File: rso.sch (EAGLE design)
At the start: 24 parts, among them X10 1-227161-0, X6 1-227161-0, X7 1-227161-0, X8 1-227161-0, X9 1-227161-0

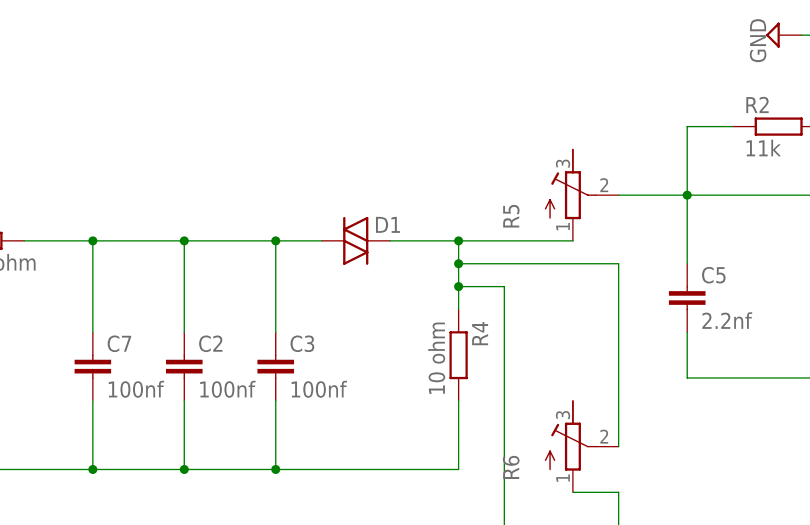
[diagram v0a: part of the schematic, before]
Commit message: CHanges to the thikness of the tracks
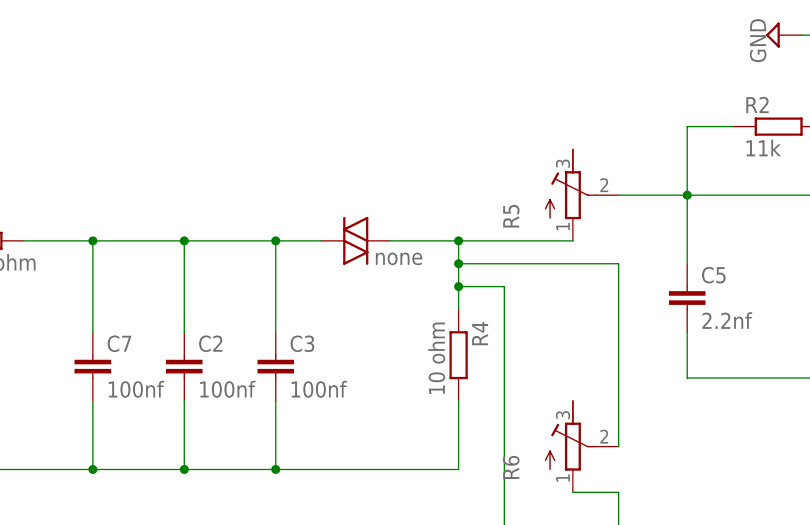
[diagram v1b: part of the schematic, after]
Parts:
- D1: value (none) -> none
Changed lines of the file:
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@@
 <classes>
 <class number="0" name="default" width="0" drill="0">
+<clearance class="0" value="0.205"/>
 </class>
 </classes>
@@
 <attribute name="RS_NUMBER" value="178-1862"/>
 </part>
-<part name="D1" library="diode" library_urn="urn:adsk.eagle:library:210" deviceset="DIAC-" device="DO35-10" package3d_urn="urn:adsk.eagle:package:43344/2">
+<part name="D1" library="diode" library_urn="urn:adsk.eagle:library:210" deviceset="DIAC-" device="DO35-10" package3d_urn="urn:adsk.eagle:package:43344/2" value="none">
 <attribute name="MF" value="NTE ELECTRONICS"/>
 <attribute name="MPN" value="NTE6408"/>
@@
 </instance>
 <instance part="D1" gate="-B1" x="-30.48" y="172.72" smashed="yes">
-<attribute name="NAME" x="-29.718" y="173.609" size="1.778" layer="95"/>
+<attribute name="NAME" x="-29.718" y="173.609" size="1.778" layer="95" display="off"/>
 <attribute name="VALUE" x="-29.718" y="170.053" size="1.778" layer="96"/>
 <attribute name="OC_FARNELL" x="-30.48" y="172.72" size="1.778" layer="96" display="off"/>
@@
 </sheet>
 </sheets>
+<errors>
+</errors>
 </schematic>
 </drawing>
